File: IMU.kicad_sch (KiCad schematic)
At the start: 0 parts

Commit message: new update
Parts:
- added C29, C30: 100nF, C0402C104K4RAC:CAPC1005X55N, symbol C0402C104K4RAC:C0402C104K4RAC
- added U1: BMI088, Module:PQFN50P450X300X100-16N, symbol BMI088:BMI088
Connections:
- new net +3V3_BMI: C29.2, C30.2, U1.11 (VDDIO), U1.3 (VDD)
- new net CSB_ACCEL: U1.14 (CSB1)
- new net CSB_GYRO: U1.5 (CSB2)
- new net GND: C29.1, C30.1, U1.2 (NC), U1.4 (GNDA), U1.6 (GNDIO), U1.7 (PS)
- new net INT1_ACCEL: U1.16 (INT1)
- new net INT1_GYRO: U1.12 (INT3)
- new net INT2_ACCEL: U1.1 (INT2)
- new net INT2_GYRO: U1.13 (INT4)
- new net MISO: U1.10 (SDO2), U1.15 (SDO1)
- new net MOSI: U1.9 (SDA/SDI)
- new net SCK: U1.8 (SCL/SCK)

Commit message: new
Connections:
- net MISO renamed SDO
- net MOSI renamed SDI
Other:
- moved on the sheet: C29, C30, U1

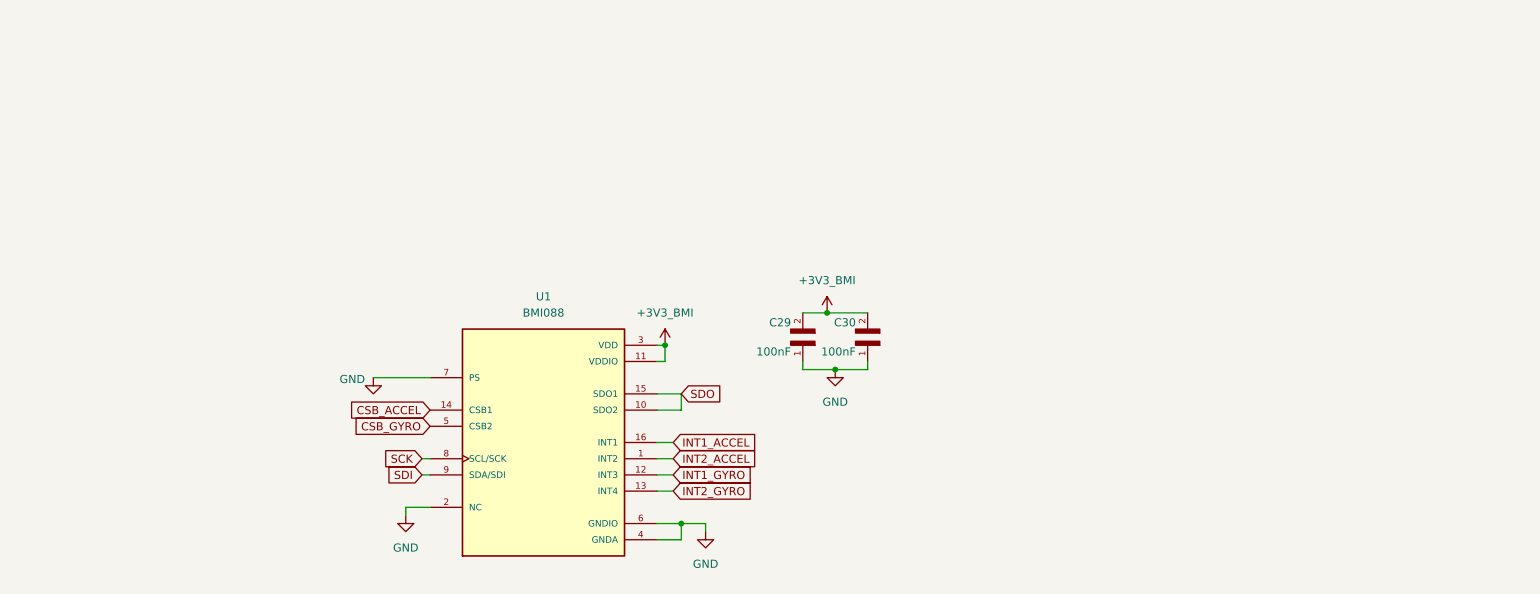
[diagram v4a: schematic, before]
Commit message: update the LED,SD card slot and new IMU
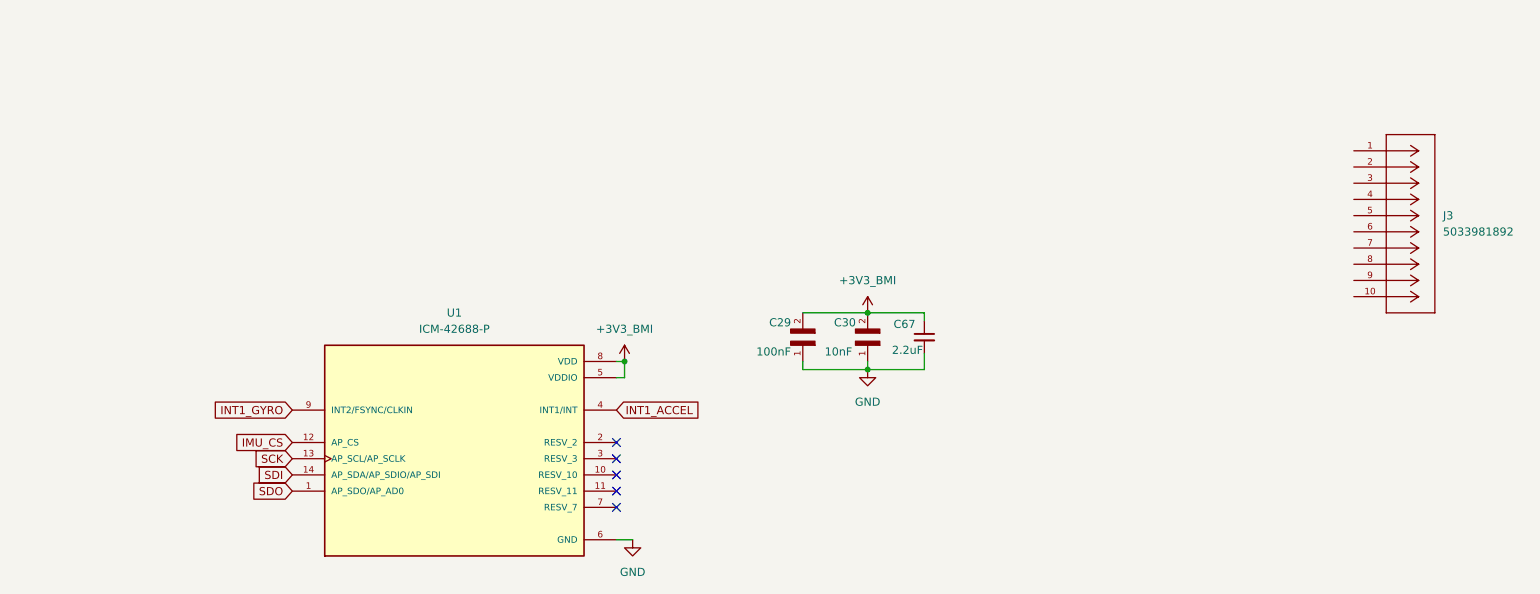
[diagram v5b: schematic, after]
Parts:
- removed U1: BMI088, Module:PQFN50P450X300X100-16N, symbol BMI088:BMI088
- added C67: 2.2uF, Capacitor_SMD:C_0805_2012Metric, symbol Device:C_Small
- added J3: 5033981892, GNSS_Library:CONN_503398-1892_MOL, symbol 5033981892:5033981892
- added U1: ICM-42688-P, ICM-42688-P:PQFN50P300X250X97-14N, symbol ICM-42688-P:ICM-42688-P
- C30: value 100nF -> 10nF
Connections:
- net +3V3_BMI: now also C67.1, U1.5 (VDDIO), U1.8 (VDD)
- net GND: now also C67.2, U1.6 (GND)
- net INT1_ACCEL: now also U1.4 (INT1/INT)
- net INT1_GYRO: now also U1.9 (INT2/FSYNC/CLKIN)
- net SCK: now also U1.13 (AP_SCL/AP_SCLK)
- net SDI: now also U1.14 (AP_SDA/AP_SDIO/AP_SDI)
- net SDO: now also U1.1 (AP_SDO/AP_AD0)
- new net IMU_CS: U1.12 (AP_CS)
- no-connect marks 0 -> 5

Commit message: filter for CAN
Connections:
- net SD_DAT2: now reaches J3.1
- net DETECT_SWITCH: now reaches J3.10
- net SD_CD: now reaches J3.2
- net SD_CMD: now reaches J3.3
- net SD_VDD: now reaches J3.4
- net SD_CLK: now reaches J3.5
- net SD_VSS: now reaches J3.6
- net SD_DAT0: now reaches J3.7
- net SD_DAT1: now reaches J3.8
- net DETECT_LEVER: now reaches J3.9
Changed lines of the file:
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@@
+		)
+	)
+	(global_label "SD_DAT0"
+		(shape input)
+		(at 243.84 78.74 180)
+		(fields_autoplaced yes)
+		(effects
+			(font
+				(size 1.27 1.27)
+			)
+			(justify right)
+		)
+		(property "Intersheetrefs" "${INTERSHEET_REFS}"
+			(at 232.872 78.74 0)
+			(effects
+				(font
+					(size 1.27 1.27)
+				)
+				(justify right)
+				(hide yes)
+			)
+		)
+	)
+	(global_label "SD_CLK"
+		(shape input)
+		(at 243.84 73.66 180)
+		(fields_autoplaced yes)
+		(effects
+			(font
+				(size 1.27 1.27)
+			)
+			(justify right)
+		)
+		(property "Intersheetrefs" "${INTERSHEET_REFS}"
+			(at 233.8396 73.66 0)
+			(effects
+				(font
+					(size 1.27 1.27)
+				)
+				(justify right)
+				(hide yes)
+			)
 		)
 	)
@@
 		)
 	)
+	(global_label "SD_CD"
+		(shape input)
+		(at 243.84 66.04 180)
+		(fields_autoplaced yes)
+		(effects
+			(font
+				(size 1.27 1.27)
+			)
+			(justify right)
+		)
+		(property "Intersheetrefs" "${INTERSHEET_REFS}"
+			(at 234.8677 66.04 0)
+			(effects
+				(font
+					(size 1.27 1.27)
+				)
+				(justify right)
+				(hide yes)
+			)
+		)
+	)
 	(global_label "IMU_CS"
 		(shape input)
@@
 		)
 	)
+	(global_label "DETECT_LEVER"
+		(shape input)
+		(at 243.84 83.82 180)
+		(fields_autoplaced yes)
+		(effects
+			(font
+				(size 1.27 1.27)
+			)
+			(justify right)
+		)
+		(property "Intersheetrefs" "${INTERSHEET_REFS}"
+			(at 227.4293 83.82 0)
+			(effects
+				(font
+					(size 1.27 1.27)
+				)
+				(justify right)
+				(hide yes)
+			)
+		)
+	)
+	(global_label "SD_DAT1"
+		(shape input)
+		(at 243.84 81.28 180)
+		(fields_autoplaced yes)
+		(effects
+			(font
+				(size 1.27 1.27)
+			)
+			(justify right)
+		)
+		(property "Intersheetrefs" "${INTERSHEET_REFS}"
+			(at 232.872 81.28 0)
+			(effects
+				(font
+					(size 1.27 1.27)
+				)
+				(justify right)
+				(hide yes)
+			)
+		)
+	)
+	(global_label "SD_VSS"
+		(shape input)
+		(at 243.84 76.2 180)
+		(fields_autoplaced yes)
+		(effects
+			(font
+				(size 1.27 1.27)
+			)
+			(justify right)
+		)
+		(property "Intersheetrefs" "${INTERSHEET_REFS}"
+			(at 233.9001 76.2 0)
+			(effects
+				(font
+					(size 1.27 1.27)
+				)
+				(justify right)
+				(hide yes)
+			)
+		)
+	)
 	(global_label "SCK"
 		(shape input)
@@
 		)
 	)
+	(global_label "DETECT_SWITCH"
+		(shape input)
+		(at 243.84 86.36 180)
+		(fields_autoplaced yes)
+		(effects
+			(font
+				(size 1.27 1.27)
+			)
+			(justify right)
+		)
+		(property "Intersheetrefs" "${INTERSHEET_REFS}"
+			(at 226.2802 86.36 0)
+			(effects
+				(font
+					(size 1.27 1.27)
+				)
+				(justify right)
+				(hide yes)
+			)
+		)
+	)
+	(global_label "SD_VDD"
+		(shape input)
+		(at 243.84 71.12 180)
+		(fields_autoplaced yes)
+		(effects
+			(font
+				(size 1.27 1.27)
+			)
+			(justify right)
+		)
+		(property "Intersheetrefs" "${INTERSHEET_REFS}"
+			(at 233.7791 71.12 0)
+			(effects
+				(font
+					(size 1.27 1.27)
+				)
+				(justify right)
+				(hide yes)
+			)
+		)
+	)
 	(global_label "SDI"
 		(shape input)
@@
 			(effects
 				(font
+					(size 1.27 1.27)
+				)
+				(justify right)
+				(hide yes)
+			)
+		)
+	)
+	(global_label "SD_DAT2"
+		(shape input)
+		(at 243.84 63.5 180)
+		(fields_autoplaced yes)
+		(effects
+			(font
+				(size 1.27 1.27)
+			)
+			(justify right)
+		)
+		(property "Intersheetrefs" "${INTERSHEET_REFS}"
+			(at 232.872 63.5 0)
+			(effects
+				(font
+					(size 1.27 1.27)
+				)
+				(justify right)
+				(hide yes)
+			)
+		)
+	)
+	(global_label "SD_CMD"
+		(shape input)
+		(at 243.84 68.58 180)
+		(fields_autoplaced yes)
+		(effects
+			(font
+				(size 1.27 1.27)
+			)
+			(justify right)
+		)
+		(property "Intersheetrefs" "${INTERSHEET_REFS}"
+			(at 233.4163 68.58 0)
+			(effects
+				(font

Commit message: new
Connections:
- net DETECT_LEVER renamed SD_DETECT
- net DETECT_SWITCH: no longer names the net of J3.10
- net SD_CD renamed SD_DAT3
- net SD_VDD: no longer names the net of J3.4
- net SD_VSS: no longer names the net of J3.6
